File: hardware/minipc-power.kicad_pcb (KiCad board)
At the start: 4 copper layers, 52 x 36 mm, 104 parts, among them J1 USB-C HRO TYPE-C-31-M-12, J10 VSYS (switch), J11 CHG, J12 PG_CHG, J13 VBAT_SENSE, J14 3V3_PG, J15 GND, J16 GND, J17 GND, J2 BAT+, J3 BAT-, J4 NTC, J5 NTC-, J6 +12V OUT, J7 +5V OUT, J8 +3V3 OUT, J9 EN (switch), Q1 CSD13202Q2, Q2 CSD13202Q2, Q3 CSD13202Q2, Q4 CSD25404Q3, Q5 CSD25404Q3, Q6 2N7002, U1 CH224Q, U2 BQ25606, U3 HY2113-MB1A, U4 TPS61178, U5 TPS61088-Q1, U6 TPS63802

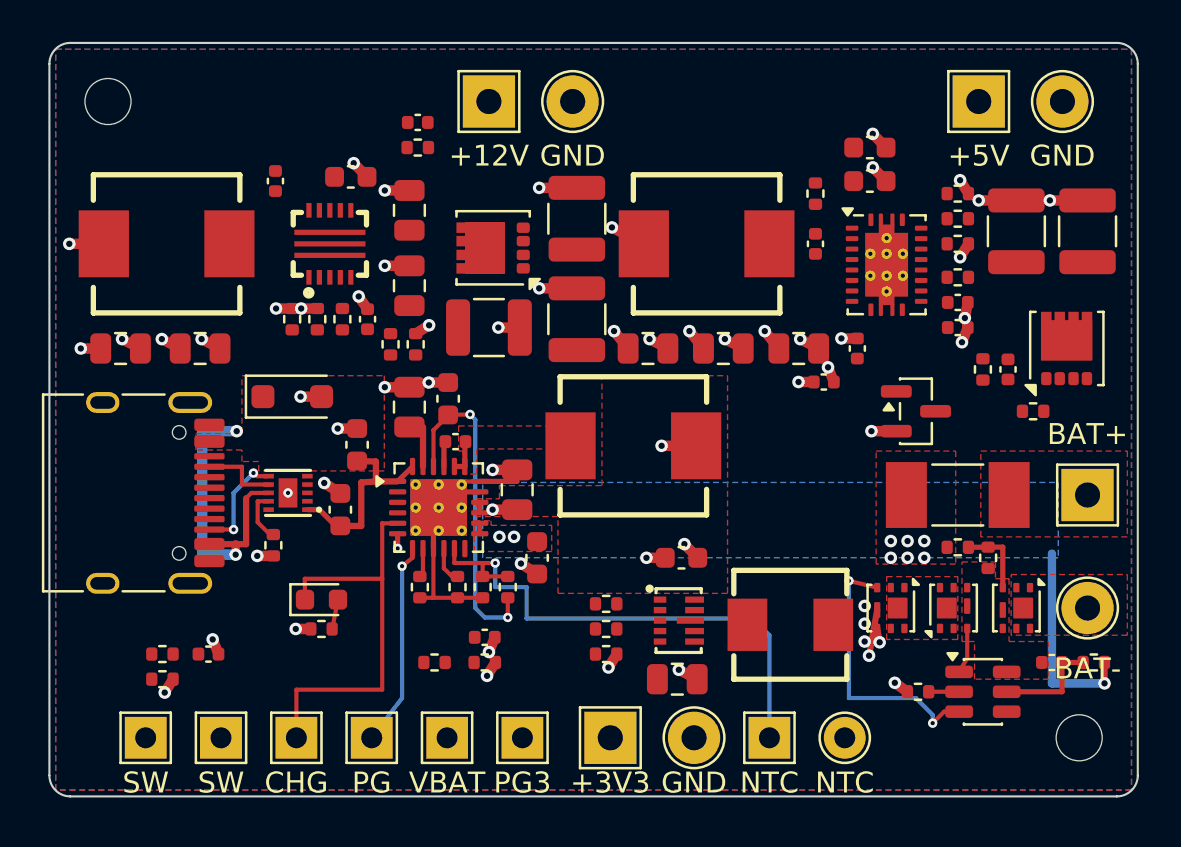
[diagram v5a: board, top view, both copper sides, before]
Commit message: Gap 22: one agent session per layout stage with a brief; 12V re-placement per fig. 36
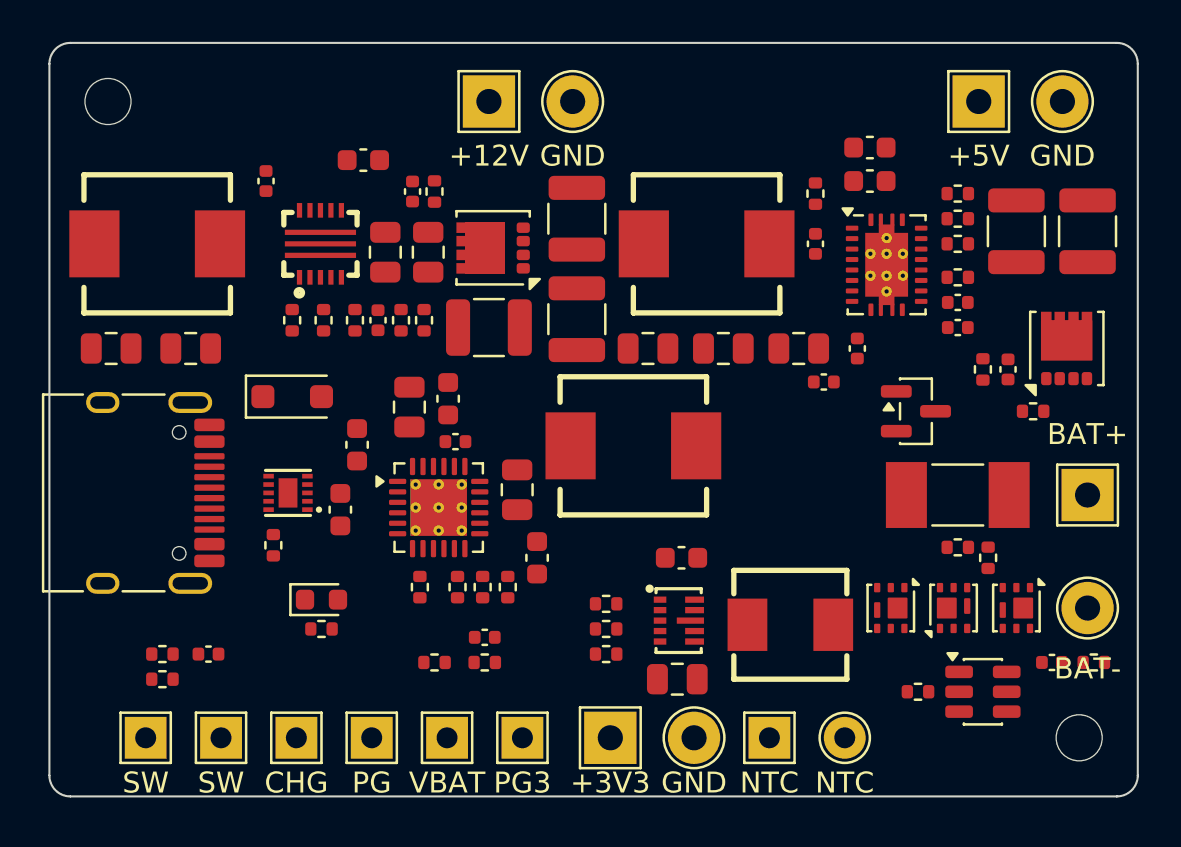
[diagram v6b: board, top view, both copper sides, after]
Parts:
- moved C16 3.31 mm to (117.3, 107.1), turned to 90 degrees
- moved C14 2.31 mm to (116.0, 110.0), turned to -90 degrees
- moved R16 2.25 mm to (118.4, 107.1), turned to 90 degrees
- moved R13 1.97 mm to (117.9, 113.2)
- moved C15 1.84 mm to (118.1, 110.0), turned to -90 degrees
- moved R14 1.35 mm to (116.8, 113.2), turned to -90 degrees
- moved C12 1.00 mm to (115.0, 105.6)
- moved R15 0.60 mm to (114.6, 113.2), turned to -90 degrees
- moved C13 0.50 mm to (115.7, 113.2), turned to -90 degrees
- moved C10 0.45 mm to (106.8, 114.6)
- moved C11 0.45 mm to (110.3, 106.6)
- moved C9 0.45 mm to (103.0, 114.6)
- moved U4 0.45 mm to (113.0, 109.6)
- moved L2 0.45 mm to (105.2, 109.6)
- moved R12 0.30 mm to (113.1, 113.2), turned to -90 degrees
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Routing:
- net GND: track 55.0 -> 0.00 mm, vias 49 -> 0
- net Net-(U2-TS): track 25.5 -> 0.00 mm, vias 1 -> 0
- net VBUS: track 24.3 -> 0.00 mm, vias 2 -> 0
- net Net-(LED1-K): track 19.8 -> 0.00 mm
- net Net-(U2-REGN): track 15.8 -> 0.00 mm, vias 2 -> 0
- net VSYS: track 14.2 -> 0.00 mm, vias 12 -> 0
- net Net-(Q3-G): track 13.2 -> 0.00 mm, vias 2 -> 0
- net BAT: track 10.2 -> 0.00 mm, vias 9 -> 0
- net /PG_CHG: track 9.76 -> 0.00 mm, vias 1 -> 0
- net Net-(U3-VDD): track 5.05 -> 0.00 mm
- net Net-(J1-CC2): track 5.03 -> 0.00 mm, vias 2 -> 0
- net Net-(J1-CC1): track 3.68 -> 0.00 mm
- net Net-(Q1-G): track 3.58 -> 0.00 mm
- net Net-(U1-CFG1): track 2.52 -> 0.00 mm
- net Net-(Q2-G): track 2.18 -> 0.00 mm
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- removed copper zone on B.Cu, net BAT
- removed copper zone on F.Cu, net BAT
- removed copper zone on B.Cu, net GND
- removed copper zone on F.Cu, net GND
- removed copper zone on In1.Cu, net GND
- removed copper zone on F.Cu, net Net-(C4-Pad2)
- removed copper zone on F.Cu, net Net-(F1-Pad1)
- removed copper zone on F.Cu, net Net-(J3-Pad1)
- removed copper zone on F.Cu, net Net-(Q2-D-Pad1)
- removed copper zone on F.Cu, net Net-(U3-VSS)
- removed copper zone on F.Cu, net VBUS
- removed copper zone on F.Cu, net VSYS
- removed copper zone on In2.Cu, net VSYS

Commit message: Route 12V boost per TPS61178 fig. 36 (COUT1 at bar ends, AGND bus, gate along top)
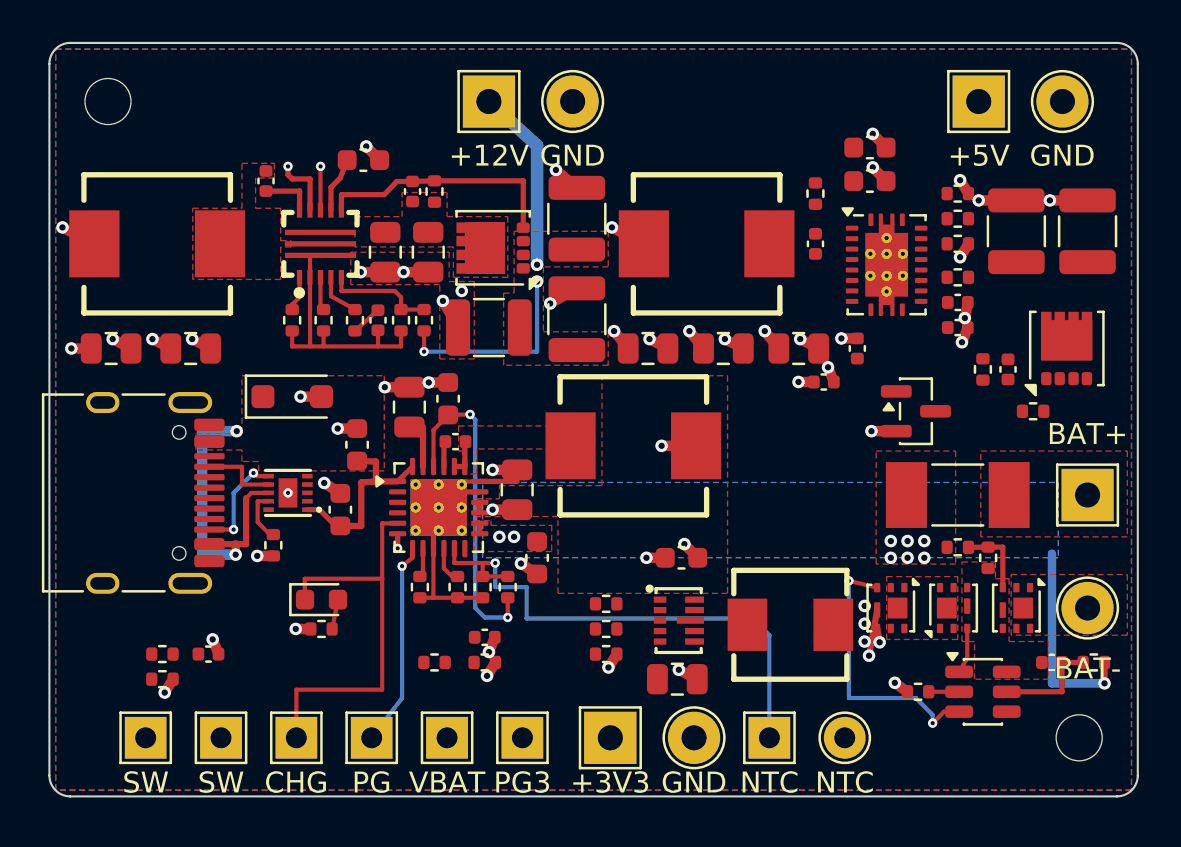
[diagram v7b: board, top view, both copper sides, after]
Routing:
- net GND: track 0.00 -> 64.1 mm, vias 0 -> 46
- net Net-(U2-TS): track 0.00 -> 25.5 mm, vias 0 -> 1
- net VBUS: track 0.00 -> 24.3 mm, vias 0 -> 2
- net Net-(LED1-K): track 0.00 -> 19.8 mm
- net +12V: track 0.00 -> 18.6 mm, vias 0 -> 3
- net VSYS: track 0.00 -> 17.3 mm, vias 0 -> 13
- net Net-(U2-REGN): track 0.00 -> 15.8 mm, vias 0 -> 2
- net Net-(Q3-G): track 0.00 -> 13.2 mm, vias 0 -> 2
- net Net-(Q4-G): track 0.00 -> 11.9 mm
- net BAT: track 0.00 -> 10.2 mm, vias 0 -> 9
- net /PG_CHG: track 0.00 -> 9.76 mm, vias 0 -> 1
- net Net-(U4-FB): track 0.00 -> 5.31 mm
- net Net-(U3-VDD): track 0.00 -> 5.05 mm
- net Net-(J1-CC2): track 0.00 -> 5.03 mm, vias 0 -> 2
- net Net-(J1-CC1): track 0.00 -> 3.68 mm
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- added copper zone on F.Cu, net +12V
- added copper zone on B.Cu, net BAT
- added copper zone on F.Cu, net BAT
- added copper zone on B.Cu, net GND
- added copper zone on F.Cu, net GND
- added copper zone on In1.Cu, net GND
- added copper zone on F.Cu, net Net-(C4-Pad2)
- added copper zone on F.Cu, net Net-(F1-Pad1)
- added copper zone on F.Cu, net Net-(J3-Pad1)
- added copper zone on F.Cu, net Net-(Q2-D-Pad1)
- added copper zone on F.Cu, net Net-(Q4-S)
- added copper zone on F.Cu, net Net-(U3-VSS)
- added copper zone on F.Cu, net Net-(U4-SW)
- added copper zone on F.Cu, net VBUS
- added copper zone on F.Cu, net VSYS
- added copper zone on In2.Cu, net VSYS

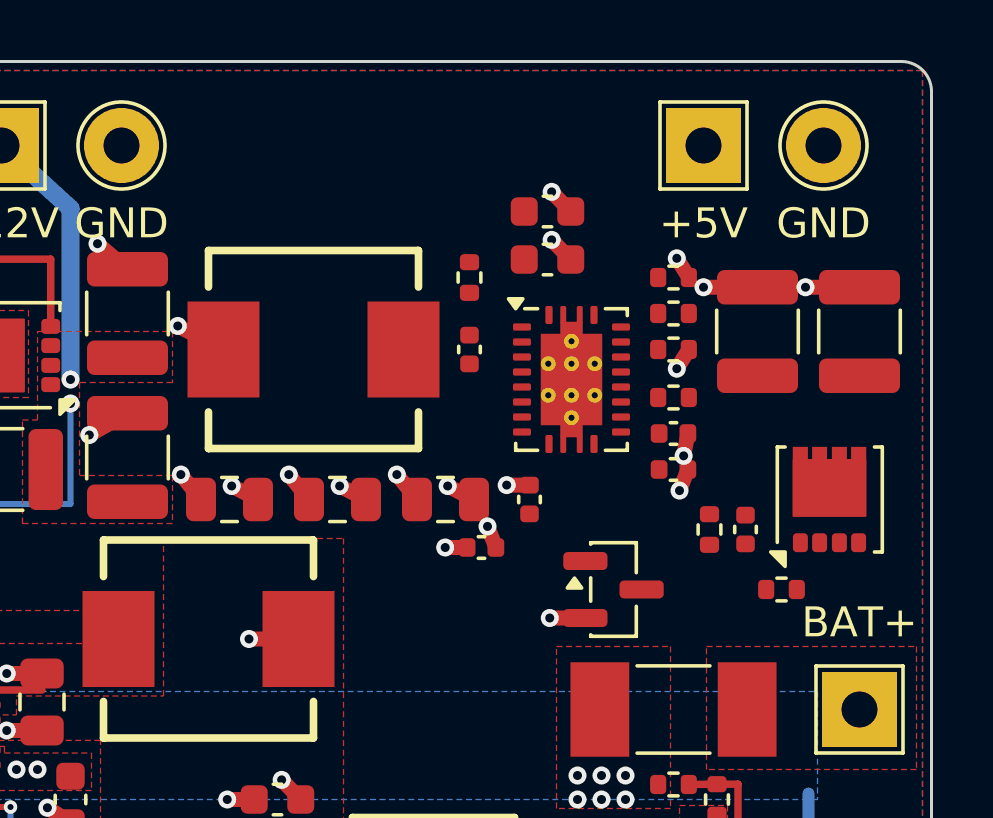
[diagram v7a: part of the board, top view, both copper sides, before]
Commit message: Route 5V boost per TPS61088-Q1 fig. 21; load switch top-right (+5V/GND top pads swapped)
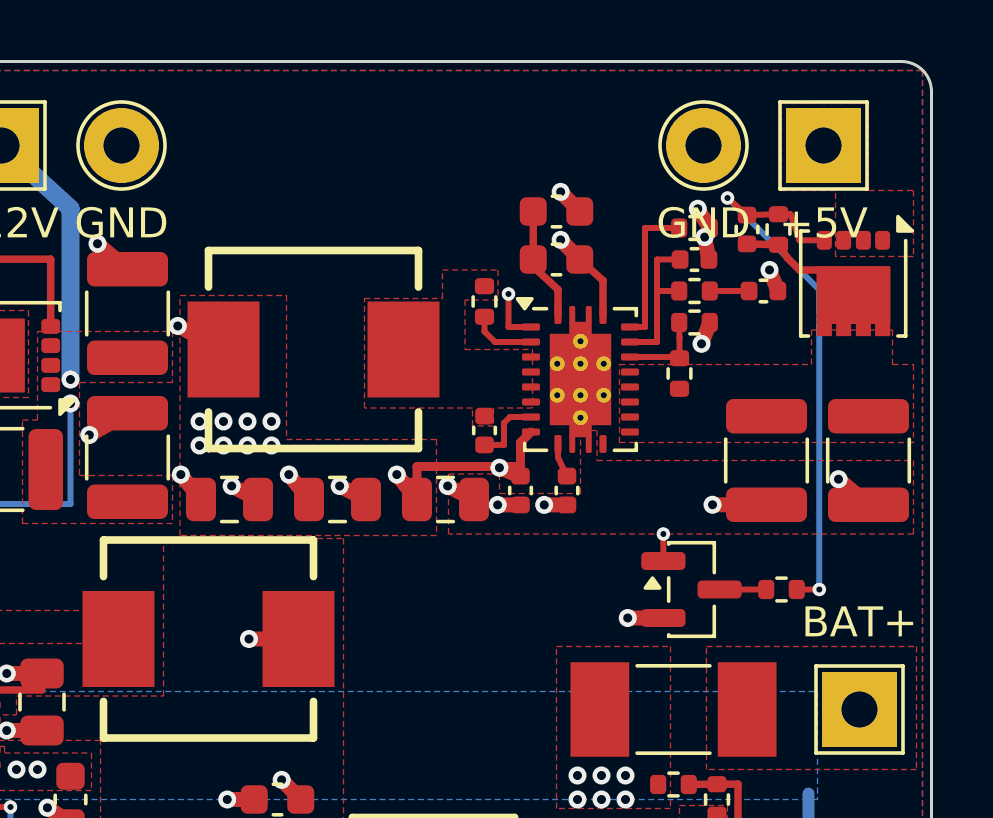
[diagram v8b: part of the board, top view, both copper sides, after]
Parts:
- moved R22 10.3 mm to (146.9, 105.6)
- moved C32 10.0 mm to (145.8, 105.6)
- moved Q5 7.24 mm to (149.4, 107.4), turned to -90 degrees
- moved C29 7.03 mm to (144.1, 106.6)
- moved C28 5.62 mm to (146.4, 107.7)
- moved C30 4.31 mm to (146.5, 113.3), turned to -90 degrees
- moved C31 4.31 mm to (149.9, 113.3), turned to -90 degrees
- moved J16 4.00 mm to (144.4, 102.8)
- moved J7 4.00 mm to (148.4, 102.8)
- moved R21 3.62 mm to (144.1, 107.7)
- moved C24 2.75 mm to (137.1, 112.3)
- moved Q6 2.60 mm to (144.0, 117.6)
- moved C23 2.30 mm to (138.3, 114.3), turned to -90 degrees
- moved R19 2.01 mm to (143.6, 110.4), turned to 90 degrees
- moved R18 1.79 mm to (144.1, 105.5)
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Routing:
- net Net-(Q5-G): track 0.00 -> 19.1 mm, vias 0 -> 2
- net VSYS: track 17.3 -> 23.5 mm, vias 13 -> 21
- net Net-(U5-COMP): track 0.00 -> 5.16 mm
- net Net-(U5-ILIM): track 0.00 -> 4.94 mm
- net Net-(U5-VCC): track 0.00 -> 3.77 mm
- net Net-(U5-FB): track 0.00 -> 2.88 mm
- net Net-(Q5-S): track 0.00 -> 2.85 mm
- net /EN: track 2.10 -> 4.85 mm, vias 1 -> 3
- net Net-(U5-BOOT): track 0.00 -> 2.36 mm
- net Net-(U5-FSW): track 0.00 -> 2.18 mm
- net GND: track 64.1 -> 65.8 mm
- net Net-(Q6-D): track 0.00 -> 1.55 mm
- net Net-(C28-Pad1): track 0.00 -> 1.31 mm
- net Net-(U5-SS): track 0.00 -> 1.14 mm
- added copper zone on F.Cu, net +5V
- added copper zone on F.Cu, net Net-(C24-Pad2)
- added copper zone on F.Cu, net Net-(Q5-S)
